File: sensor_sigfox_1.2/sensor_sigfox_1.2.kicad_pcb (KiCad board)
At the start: 2 copper layers, 27.3 x 60.1 mm, 15 parts, among them IC1 WSSFM11R2DAT, J1 Battery, J2 Conn_01x07_Socket, U1 ATtiny826-X, U2 MLX90393, Y1 32.768 kHz

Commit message: gerber y conexiones int/trig
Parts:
- moved C1 0.99 mm to (121.2, 88.9)
- moved C2 0.99 mm to (121.2, 90.8)
- moved J1 0.37 mm to (116.4, 77.1)
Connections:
- U1 pad 2: unconnected-(U1-PA3-Pad2) -> Net-(U1-PA3)
- U1 pad 5: unconnected-(U1-PA4-Pad5) -> Net-(U1-PA4)
- U2 pad 1: unconnected-(U2-INT-Pad1) -> Net-(U1-PA3)
- U2 pad 7: unconnected-(U2-INT/TRIG-Pad7) -> Net-(U1-PA4)
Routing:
- net Net-(U1-PA3): track 0.00 -> 63.8 mm, vias 0 -> 2
- net Net-(U1-PA4): track 0.00 -> 60.8 mm, vias 0 -> 2
- net GND: track 132.6 -> 130.8 mm
- net /SF_TX: track 27.6 -> 28.5 mm
- net Net-(J2-Pin_3): track 12.7 -> 13.5 mm
- net /SDA: track 95.7 -> 96.4 mm

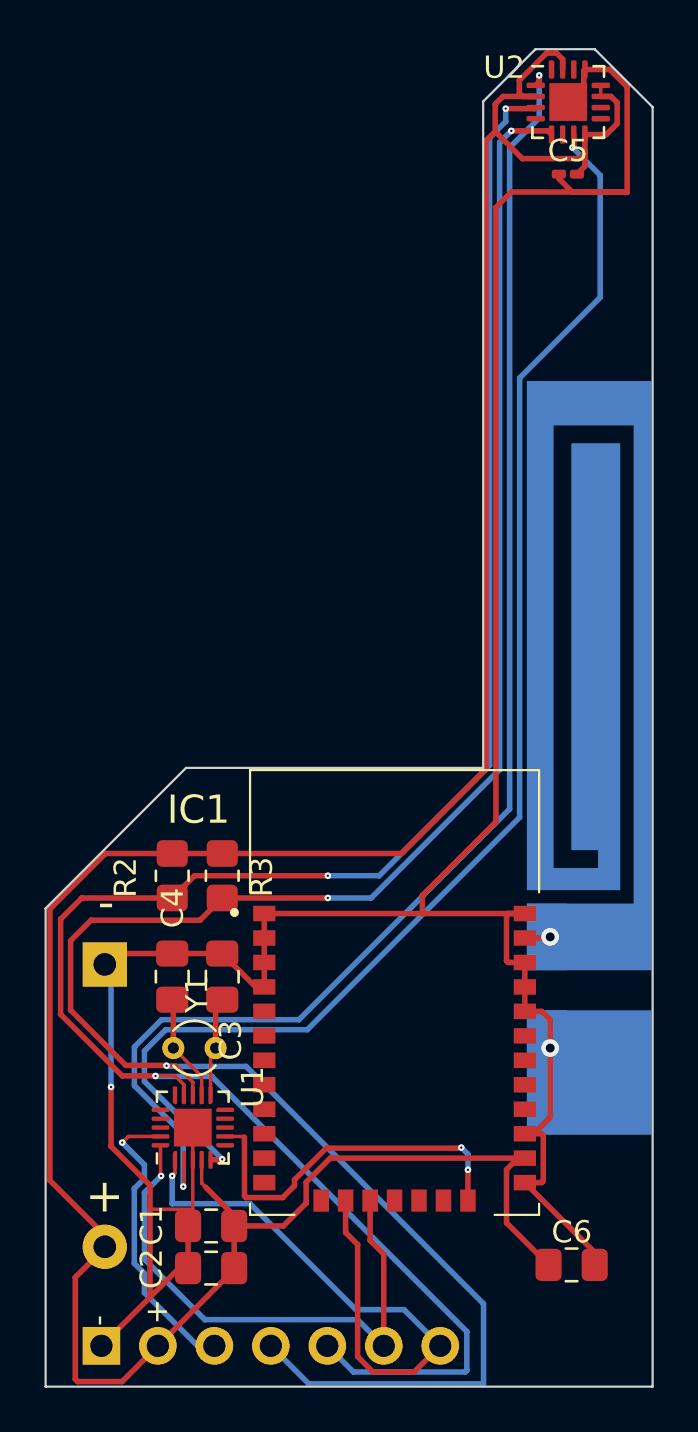
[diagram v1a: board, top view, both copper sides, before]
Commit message: 1.1 y 1.2 actualizados
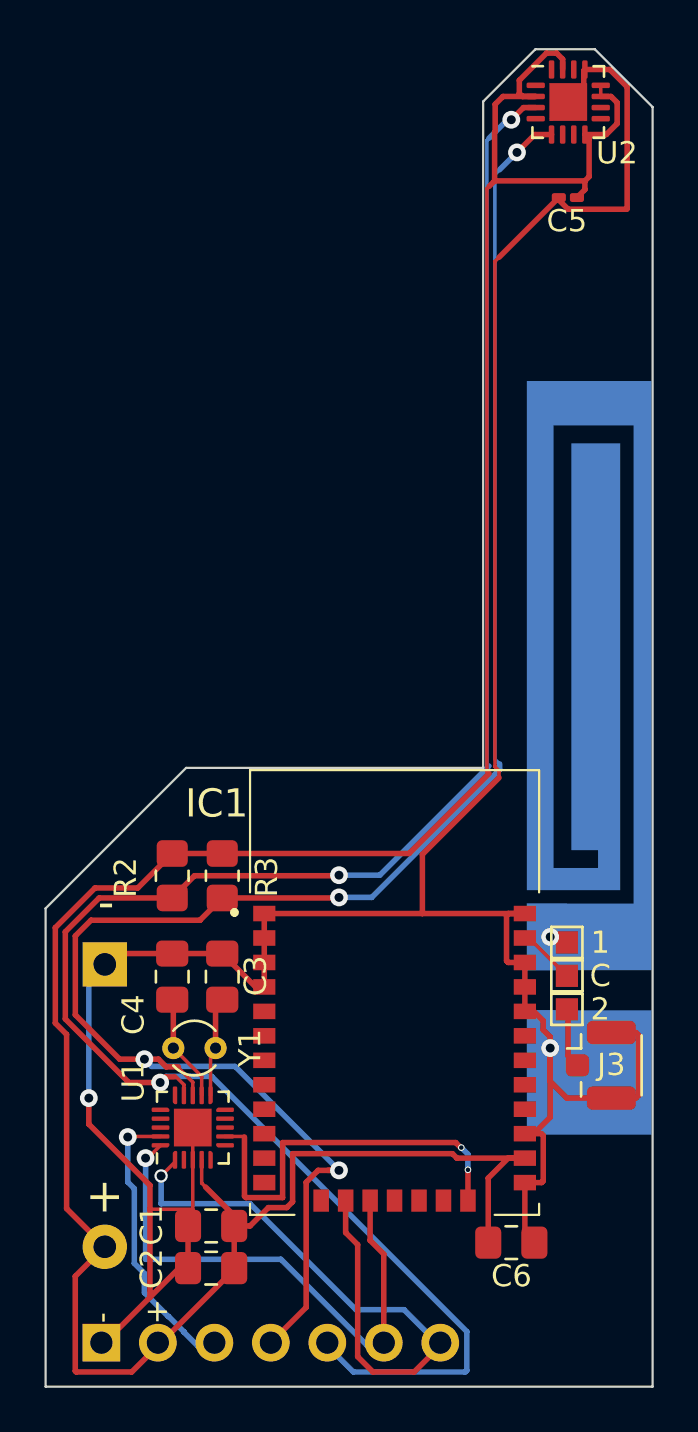
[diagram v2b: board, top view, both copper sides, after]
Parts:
- added 1: TestPoint, TestPoint:TestPoint_Pad_1.0x1.0mm, F.Cu at (137.2, 76.1)
- added 2: TestPoint, TestPoint:TestPoint_Pad_1.0x1.0mm, F.Cu at (137.2, 79.1)
- added C: TestPoint, TestPoint:TestPoint_Pad_1.0x1.0mm, F.Cu at (137.2, 77.6)
- added J3: Conn_Coaxial, Connector_Coaxial:U.FL_Hirose_U.FL-R-SMT-1_Vertical, F.Cu at (138.7, 81.7)
- moved C6 2.89 mm to (134.7, 89.6)
- moved C5 1.05 mm to (137.2, 42.6)
- moved J2 0.14 mm to (116.2, 94.1)
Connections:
- IC1 pad 30: Net-(AE1-A) -> Net-(IC1-RF_IO)
- U1 pad 2: Net-(U1-PA3) -> unconnected-(U1-PA3-Pad2)
- U1 pad 5: Net-(U1-PA4) -> unconnected-(U1-PA4-Pad5)
- U2 pad 1: Net-(U1-PA3) -> unconnected-(U2-INT-Pad1)
- U2 pad 7: Net-(U1-PA4) -> unconnected-(U2-INT/TRIG-Pad7)
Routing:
- net Net-(U1-PA3): track 63.8 -> 0.00 mm, vias 2 -> 0
- net Net-(U1-PA4): track 60.8 -> 0.00 mm, vias 2 -> 0
- net /SDA: track 96.4 -> 84.7 mm, vias 3 -> 4
- net GND: track 130.8 -> 134.9 mm
- net Net-(J3-In): track 0.00 -> 2.69 mm
- net Net-(IC1-RF_IO): track 0.00 -> 2.59 mm
- net Net-(IC1-RST_N): track 16.9 -> 18.4 mm
- net VCC: track 128.0 -> 126.9 mm
- net /SCL: track 92.3 -> 91.5 mm
- net /SF_TX: track 28.5 -> 29.2 mm
- net Net-(J2-Pin_3): track 13.5 -> 12.9 mm
